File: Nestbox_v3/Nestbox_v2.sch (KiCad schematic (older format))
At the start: 0 parts

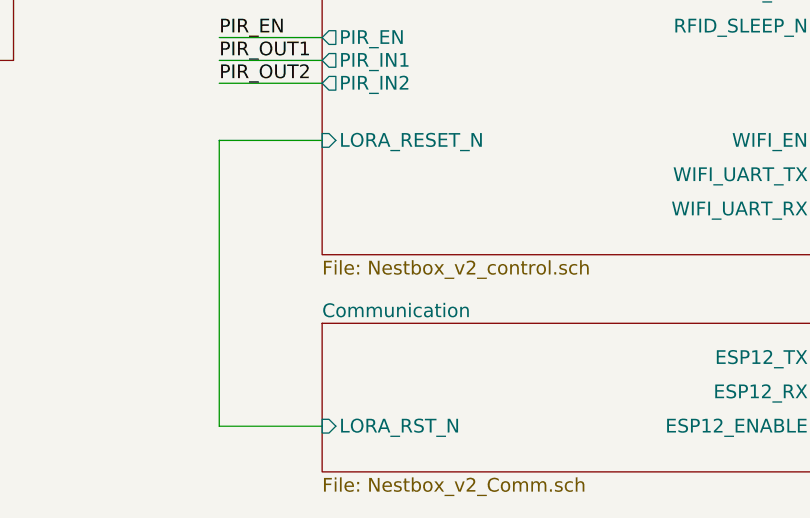
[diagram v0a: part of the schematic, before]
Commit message: production status nestbox v3
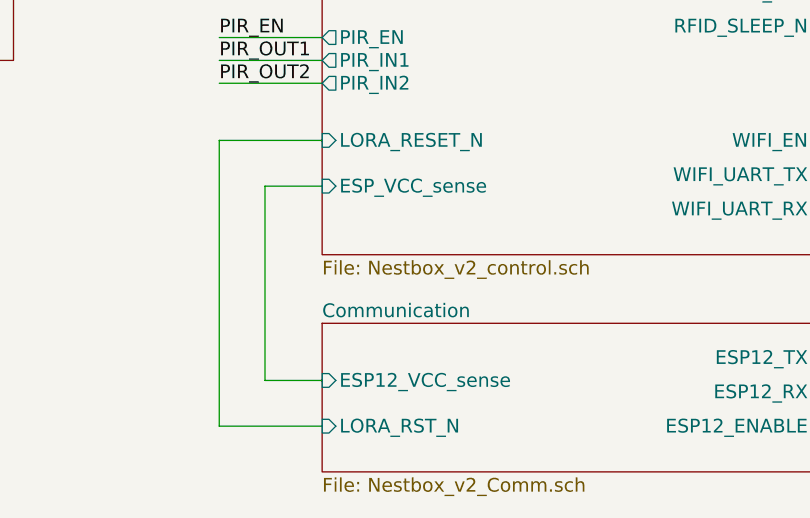
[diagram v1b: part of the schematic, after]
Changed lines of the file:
@@
 F27 "PIR_IN1" O L 5450 4150 60
 F28 "PIR_IN2" O L 5450 4250 60
+F29 "ESP_VCC_sense" I L 5450 4700 60
 $EndSheet
 $Sheet
@@
 F4 "ESP12_ENABLE" I R 7650 5750 60
 F5 "LORA_RST_N" I L 5450 5750 60
+F6 "ESP12_VCC_sense" I L 5450 5550 60
 $EndSheet
 $Sheet
@@
 Text Label 7350 1800 0    60   ~ 0
 PIR_OUT2
+Wire Wire Line
+	5450 4700 5200 4700
+Wire Wire Line
+	5200 4700 5200 5550
+Wire Wire Line
+	5200 5550 5450 5550
 $EndSCHEMATC
